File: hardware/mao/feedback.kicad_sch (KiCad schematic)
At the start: 21 parts, among them J501 SPK+, J502 SPK-, J503 LRA, Q501 AO3400A, U501 MAX98357AETE+T, U502 DRV2605LDGSR, U503 IRM-H638T/TR2

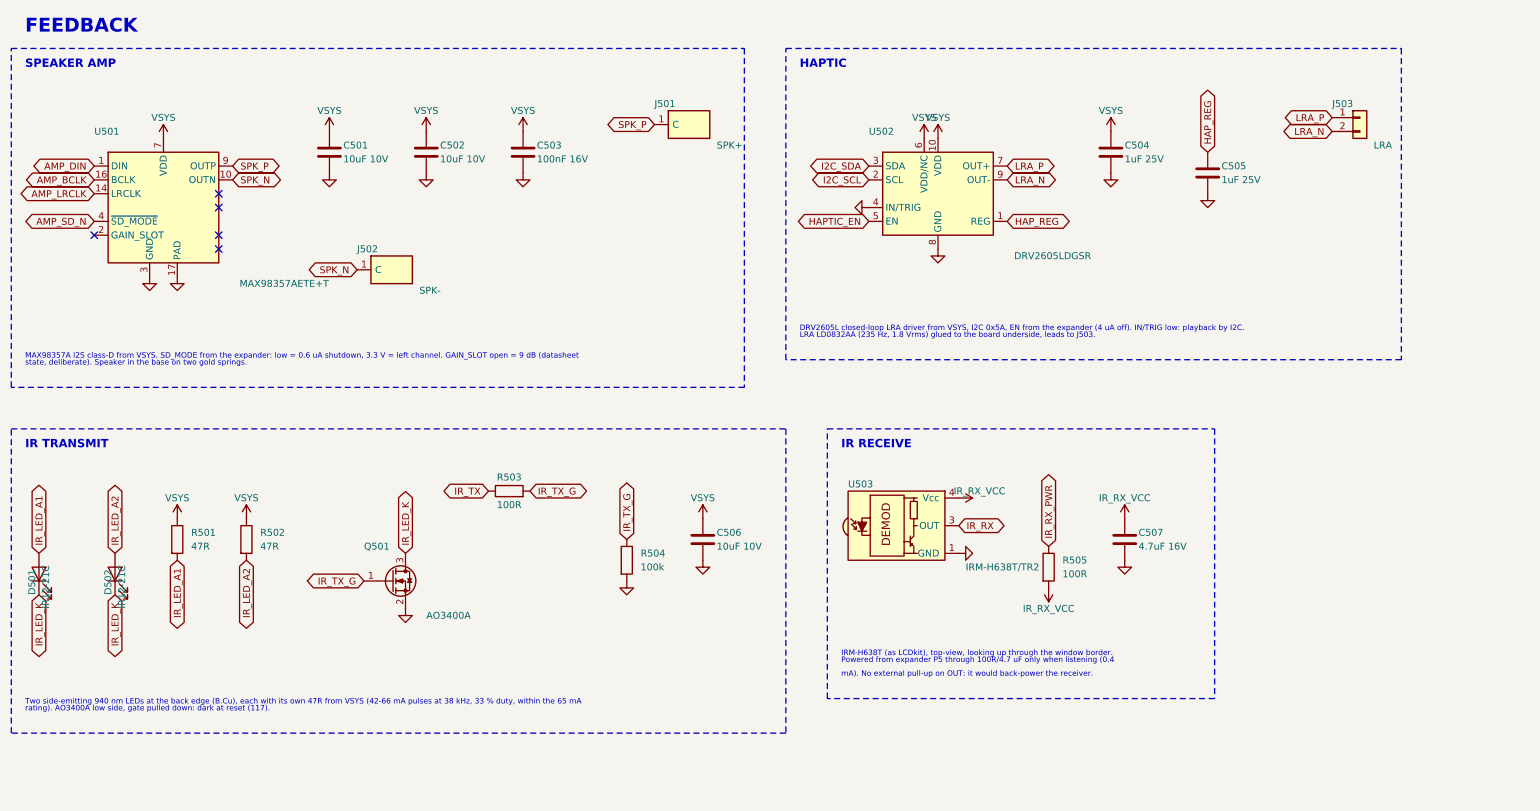
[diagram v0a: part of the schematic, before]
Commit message: hardware: MAO_MAIN A0 routed board, fab package and final review
6-layer JLC06161H-3313 board (F / GND / signals / +3V3 / GND / B), routed from the
design scripts: designed power and fan-out copper, grid router with closed-set A*,
stub pruning, GND stitching (two ties on large pour fragments), tidy.
DRC 0 violations / 0 unconnected / 0 parity; ERC 0; silkscreen checker 0 findings.

- silkscreen: ODD JOBS mark and identity on both faces, S/N box, function-named
  test pads in a 3.0 x 3.2 mm service field; references for every semiconductor and
  connector plus the passives the service docs name, the rest on assembly drawings
- stackup, black mask, white legend and ENIG written into the board
- fab: 6-layer Gerbers + drill, JLC BOM (47 lines, LCSC on every line) and CPL
  (113 parts), assembly PDFs, FAB-NOTES with computed via counts
- docs: PCB, ODD JOBS and order-readiness review sections, final report, renders,
  factory-test pad map, bring-up and architecture updates

Co-Authored-By: Claude Opus 5.5 <noreply@anthropic.com>
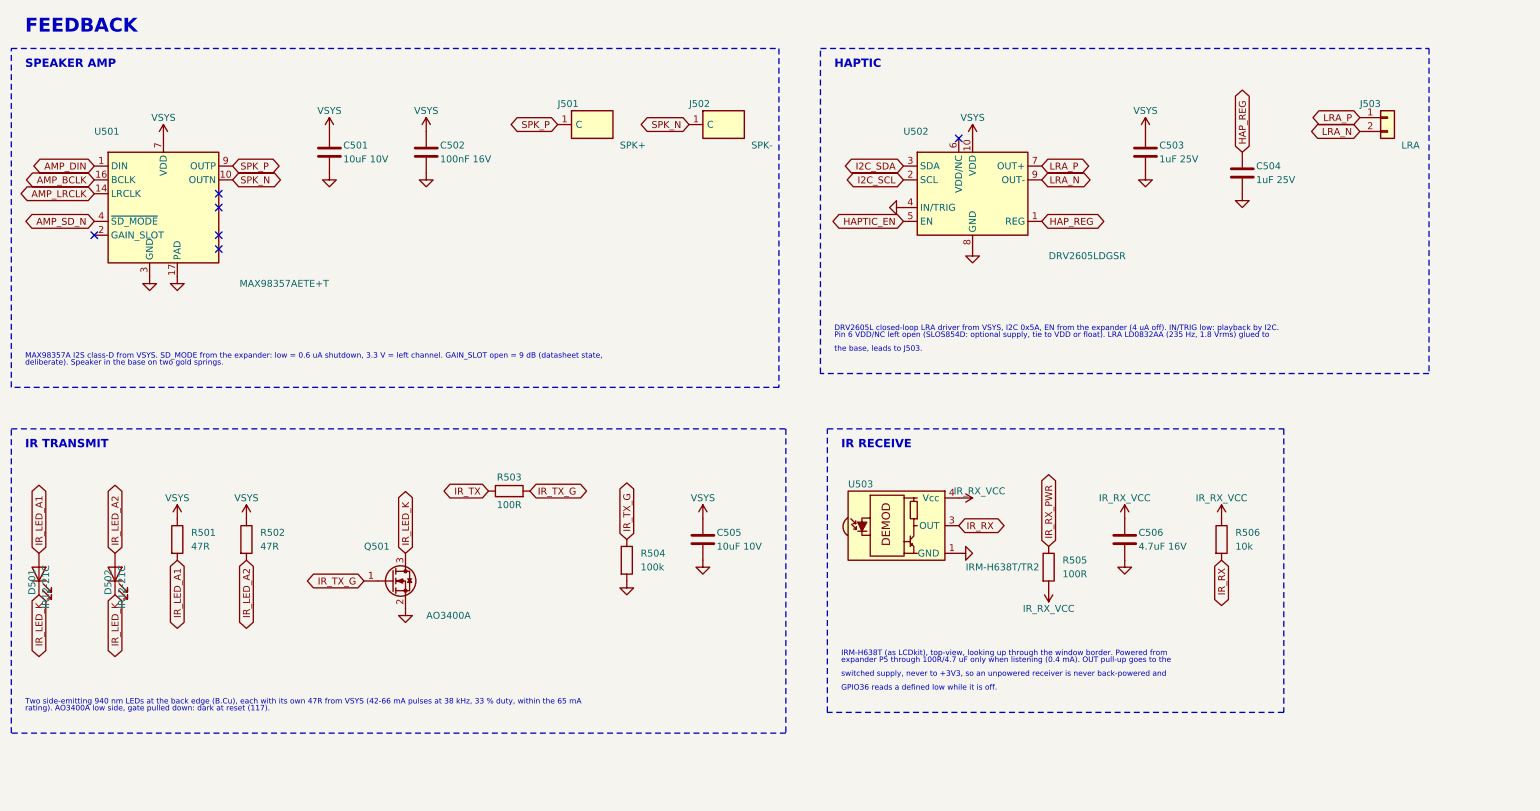
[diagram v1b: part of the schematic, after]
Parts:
- removed C507: 4.7uF 16V, Capacitor_SMD:C_0603_1608Metric, symbol Device:C
- added R506: 10k, Resistor_SMD:R_0402_1005Metric, symbol Device:R
- C502: value 10uF 10V -> 100nF 16V; footprint Capacitor_SMD:C_0603_1608Metric -> Capacitor_SMD:C_0402_1005Metric; LCSC C19702 -> C1525; MPN CL10A106KP8NNNC -> CL05B104KO5NNNC
- C503: value 100nF 16V -> 1uF 25V; LCSC C1525 -> C52923; MPN CL05B104KO5NNNC -> CL05A105KA5NQNC
- C505: value 1uF 25V -> 10uF 10V; footprint Capacitor_SMD:C_0402_1005Metric -> Capacitor_SMD:C_0603_1608Metric; LCSC C52923 -> C19702; MPN CL05A105KA5NQNC -> CL10A106KP8NNNC
- C506: value 10uF 10V -> 4.7uF 16V; LCSC C19702 -> C19666; MPN CL10A106KP8NNNC -> CL10A475KO8NNNC
- R501, R502: LCSC (none) -> C23182; MPN (none) -> 0603WAF470JT5E; Manufacturer (none) -> UNI-ROYAL
- R503, R505: LCSC (none) -> C25076; MPN (none) -> 0402WGF1000TCE; Manufacturer (none) -> UNI-ROYAL
- U501: footprint Package_DFN_QFN:TQFN-16-1EP_3x3mm_P0.5mm_EP1.23x1.23mm -> Package_DFN_QFN:TQFN-16-1EP_3x3mm_P0.5mm_EP1.23x1.23mm_ThermalVias
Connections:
- net HAP_REG: now also C504.1; no longer C505.1
- net IR_RX: now also R506.2
- net IR_RX_VCC: now also C506.1, R506.1
- net VSYS: now also C505.1; no longer C504.1, C506.1, U502.6 (VDD/NC)
- no-connect marks 5 -> 6
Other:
- note added: "GPIO36 reads a defined low while it is off."
- note added: "IRM-H638T (as LCDkit), top-view, looking up through the window border. Powered from"
- note added: "MAX98357A I2S class-D from VSYS. SD_MODE from the expander: low = 0.6 uA shutdown, 3.3 V = left channel. GAIN_SLOT open = 9 dB (datasheet state,"
- note added: "Pin 6 VDD/NC left open (SLOS854D: optional supply, tie to VDD or float). LRA LD0832AA (235 Hz, 1.8 Vrms) glued to"
- note added: "deliberate). Speaker in the base on two gold springs."
- note added: "expander P5 through 100R/4.7 uF only when listening (0.4 mA). OUT pull-up goes to the"
- note added: "switched supply, never to +3V3, so an unpowered receiver is never back-powered and"
- note added: "the base, leads to J503."
- note removed: "IRM-H638T (as LCDkit), top-view, looking up through the window border."
- note removed: "LRA LD0832AA (235 Hz, 1.8 Vrms) glued to the board underside, leads to J503."
- note removed: "MAX98357A I2S class-D from VSYS. SD_MODE from the expander: low = 0.6 uA shutdown, 3.3 V = left channel. GAIN_SLOT open = 9 dB (datasheet"
- note removed: "Powered from expander P5 through 100R/4.7 uF only when listening (0.4"
- note removed: "mA). No external pull-up on OUT: it would back-power the receiver."
- note removed: "state, deliberate). Speaker in the base on two gold springs."
- moved on the sheet: C503, C504, C505, C506, J501, J502, J503, U502

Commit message: hardware: MAO_MAIN A0 4-layer release, plug-in display, ODD JOBS review
- 4 layers (JLC04161H-1080): L1 parts + critical lines, L2 solid GND,
  L3 power regions + slow lines, L4 parts + lines. Re-placed and
  re-routed from scratch: 191 vias (6-layer board: 230).
- J301 HDGC 0.5K-HX-18PWB (C2919497): the round panel plugs in, no
  solder (Winstar 18-pin standard); display TE line added.
- 4-layer pin map; firmware header, pin-map doc and schematic notes
  generated from pinmap.py.
- Pipeline steps: power_regions, plane_check, via_off_pad, snap45 (all
  segments 0/45/90), models3d (datasheet-height bodies for every part).
- Checks: DRC/ERC/parity 0, every L2/L3 plane one piece, silk checker 0,
  Gerbers reviewed independently, firmware 5 configs 0 warnings.
- Mechanical: display standoff 2.7 mm for IR-receiver clearance, ToF
  light-blocking gasket, mic gasket tube, TOP-spring boss; panel tabs at
  2 and 8 o'clock.
- Docs: 4-layer design review, 200-rule ODD JOBS compliance, final
  report, layer plots, Gerber sheet, renders.

Co-Authored-By: Claude Opus 5.5 <noreply@anthropic.com>
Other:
- note added: "GPIO40 reads a defined low while it is off."
- note removed: "GPIO36 reads a defined low while it is off."
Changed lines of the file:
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@@
 		)
 	)
-	(text "GPIO36 reads a defined low while it is off."
+	(text "GPIO40 reads a defined low while it is off."
 		(exclude_from_sim no)
 		(at 165.1 138.43 0)

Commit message: MAO A0: speaker that fits, antenna-safe ring, flexure face, haptic input
- Speaker: the specified 15 mm round part did not fit beside the cell. Now a
  Same Sky CMS-150803-088S-X8 (15 x 8 x 3 mm) under the board at 9 o'clock;
  springs J501/J502 replaced by its contact pads LS501 (courtyard keeps B parts
  out). C501/C502 move to F above the amplifier, fed by one via into the L3
  VSYS band; speaker lines are two nested L's on B; LRA pads renamed J501.
- Touch arcs stitched at their ends (2 holes) so none sits under the speaker.
- Ring dial: 30-pole flexible ferrite strip instead of NdFeB discs, so no
  metal sweeps over the antenna; detents are LRA ticks.
- Face: rocks on its lip on three printed flexures (no sliding fit); TOP
  spring boss raised for rim presses.
- Firmware: haptic tick per dial step, click per face press; LEFT touch zone
  holds while the speaker amplifier runs.
- Board rebuilt by the pipeline: DRC/ERC/parity 0, planes one piece,
  194 vias, silk 0 findings, all segments 45 deg; fab, plots, renders and
  Gerber review regenerated. Pipeline rebuilds the footprint cache in place.
- Docs: mechanical spec, review, ODD JOBS compliance, final report,
  bring-up and factory test updated.

Co-Authored-By: Claude Opus 5.5 <noreply@anthropic.com>
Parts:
- removed J502: SPK-, MAO:BAT_BW0019BG_SpringContact_3.5x1.5mm, symbol MAO:Spring
- removed J503: LRA, MAO:WirePads_1x02_P2.5mm_1.0x1.8mm, symbol Connector_Generic:Conn_01x02
- added LS501: CMS-150803-088S-X8, MAO:SameSky_CMS-150803_SpringPads, symbol Device:Speaker
- J501: value SPK+ -> LRA; footprint MAO:BAT_BW0019BG_SpringContact_3.5x1.5mm -> MAO:WirePads_1x02_P2.5mm_1.0x1.8mm; symbol MAO:Spring -> Connector_Generic:Conn_01x02; Exclude from BOM (none) -> yes; LCSC C2826516 -> (none); MPN BW0019BG-L3.5W1.5H3.8 -> PCB feature: LD0832AA-0099F leads; Manufacturer BAT WIRELESS -> (none); now left out of the parts list
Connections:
- net LRA_N: now also J501.2 (Pin_2)
- net LRA_P: now also J501.1 (Pin_1)
- net SPK_N: now also LS501.2
- net SPK_P: now also LS501.1; no longer J501.1 (C)
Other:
- note added: "9 o'clock; its own spring contacts press on two pads on B.Cu (LS501)."
- note added: "= 9 dB (datasheet state, deliberate). Speaker: Same Sky CMS-150803-088S-X8 (15 x 8 x 3 mm, 8 ohm, 0.8 W) in the base at"
- note added: "MAX98357A I2S class-D from VSYS. SD_MODE from the expander: low = 0.6 uA shutdown, 3.3 V = left channel. GAIN_SLOT open"
- note added: "the base, leads to J501."
- note removed: "MAX98357A I2S class-D from VSYS. SD_MODE from the expander: low = 0.6 uA shutdown, 3.3 V = left channel. GAIN_SLOT open = 9 dB (datasheet state,"
- note removed: "deliberate). Speaker in the base on two gold springs."
- note removed: "the base, leads to J503."
- moved on the sheet: C503, C504, C505, C506, D501, D502, Q501, R501, R502, R503, R504, R505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

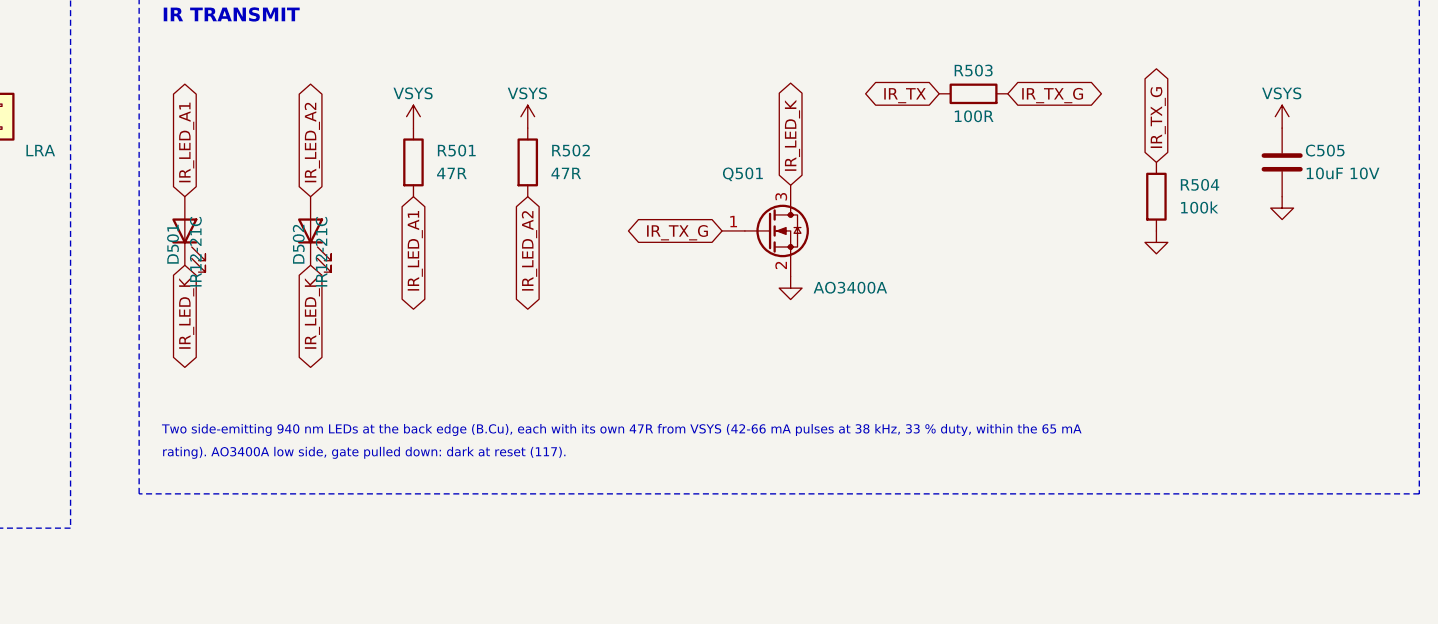
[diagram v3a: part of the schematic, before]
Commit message: MAO A0: circuit simulation suite and the value fixes it found
- hardware/mao/sim: ngspice (KiCad libngspice) + Python suite S1-S15 with
  plots in docs/hardware/sim and results in mao-a0-verification.md
- UVLO divider 470k/240k (was 1M/510k): EN leakage put the worst-case
  cut-off at 2.65 V; now 2.75-3.16 V
- IR LED resistors 56R (was 47R): peaks were 66-70 mA on USB against the
  65 mA rating; now <= 59 mA
- Firmware: 100 % brightness = 80 % backlight PWM, so the 2.8 V panel bin
  averages <= 40 mA
- Docs: speaker power 0.54 W (was quoted as 0.4 W), UVLO, IR, budget,
  bring-up checks for the backlight bin and the ring strip field
- Capture reports fitted and DNP parts separately

Co-Authored-By: Claude Opus 5.5 <noreply@anthropic.com>
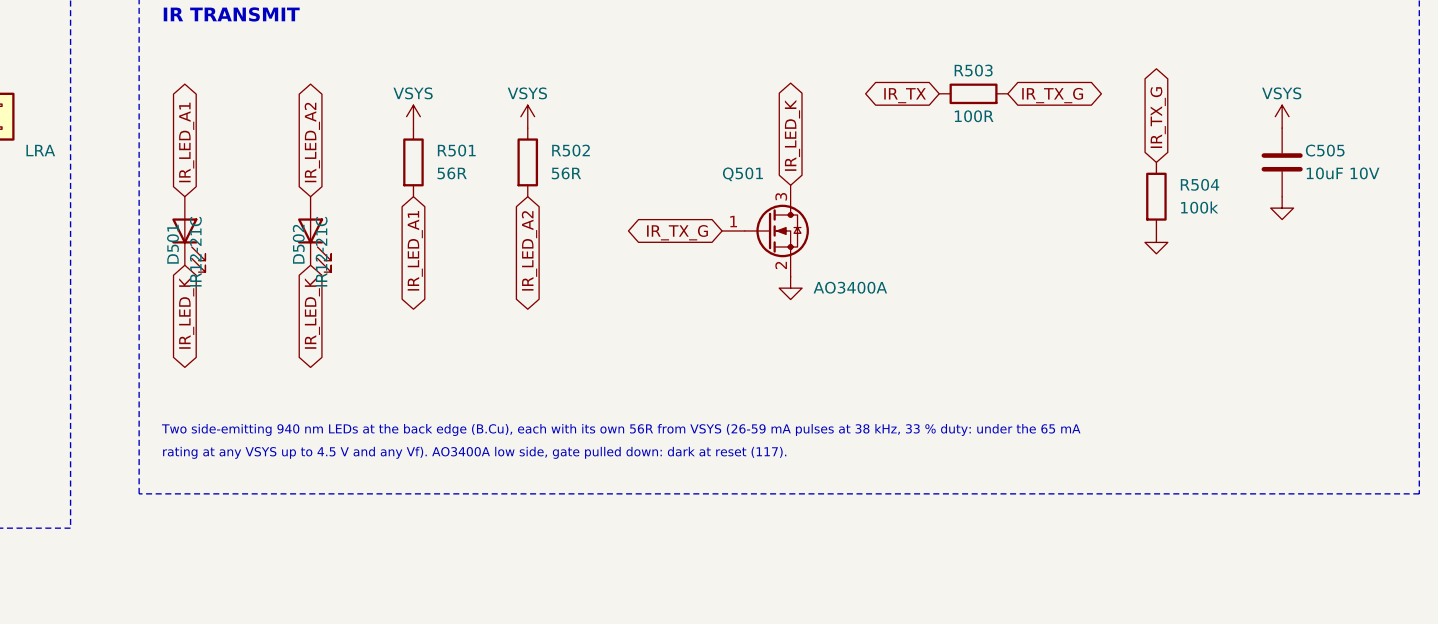
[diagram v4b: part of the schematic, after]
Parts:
- R501, R502: value 47R -> 56R; LCSC C23182 -> C25196; MPN 0603WAF470JT5E -> 0603WAF560JT5E
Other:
- note added: "Two side-emitting 940 nm LEDs at the back edge (B.Cu), each with its own 56R from VSYS (26-59 mA pulses at 38 kHz, 33 % duty: under the 65 mA"
- note added: "rating at any VSYS up to 4.5 V and any Vf). AO3400A low side, gate pulled down: dark at reset (117)."
- note removed: "Two side-emitting 940 nm LEDs at the back edge (B.Cu), each with its own 47R from VSYS (42-66 mA pulses at 38 kHz, 33 % duty, within the 65 mA"
- note removed: "rating). AO3400A low side, gate pulled down: dark at reset (117)."
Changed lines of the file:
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@@
 		)
 	)
-	(text "Two side-emitting 940 nm LEDs at the back edge (B.Cu), each with its own 47R from VSYS (42-66 mA pulses at 38 kHz, 33 % duty, within the 65 mA"
+	(text "Two side-emitting 940 nm LEDs at the back edge (B.Cu), each with its own 56R from VSYS (26-59 mA pulses at 38 kHz, 33 % duty: under the 65 mA"
 		(exclude_from_sim no)
 		(at 257.81 69.85 0)
@@
 		)
 	)
-	(text "rating). AO3400A low side, gate pulled down: dark at reset (117)."
+	(text "rating at any VSYS up to 4.5 V and any Vf). AO3400A low side, gate pulled down: dark at reset (117)."
 		(exclude_from_sim no)
 		(at 257.81 72.39 0)
@@
 			)
 		)
-		(property "Value" "47R"
+		(property "Value" "56R"
 			(at 288.29 40.64 0)
 			(effects
@@
 			)
 		)
-		(property "MPN" "0603WAF470JT5E"
+		(property "MPN" "0603WAF560JT5E"
 			(at 285.75 39.37 0)
 			(effects
@@
 			)
 		)
-		(property "LCSC" "C23182"
+		(property "LCSC" "C25196"
 			(at 285.75 39.37 0)
 			(effects
@@
 			)
 		)
-		(property "Value" "47R"
+		(property "Value" "56R"
 			(at 300.99 40.64 0)
 			(effects
@@
 			)
 		)
-		(property "MPN" "0603WAF470JT5E"
+		(property "MPN" "0603WAF560JT5E"
 			(at 298.45 39.37 0)
 			(effects
@@
 			)
 		)
-		(property "LCSC" "C23182"
-			(at 298.45 39.37 0)
-			(effects
+		(property "LCSC" "C25196"
+			(at 298.45 39.37 0)
+			(effects
